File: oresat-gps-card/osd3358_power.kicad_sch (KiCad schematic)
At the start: 52 parts, among them Q6 MMBT2907, U1 OSD3358-512M-BSM, U10 SN74LVC1G07DCK, U13 RCLAMP0504FB, U14 TLVH431

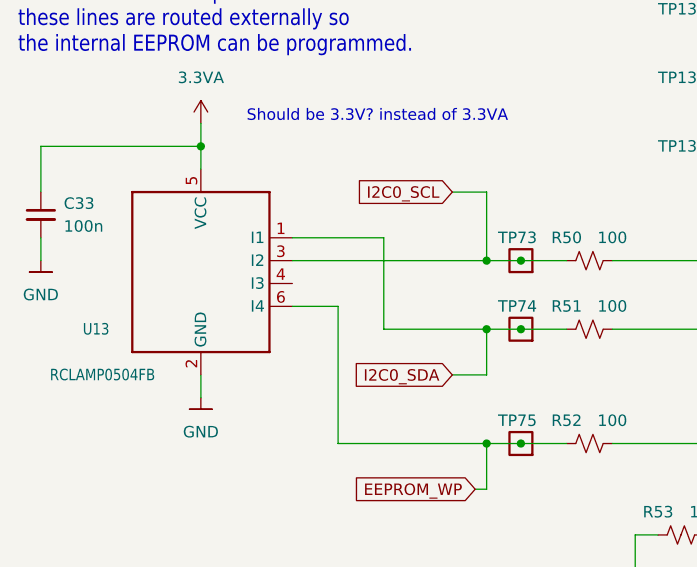
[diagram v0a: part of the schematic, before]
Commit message: GPS card design review changes and issue fixes
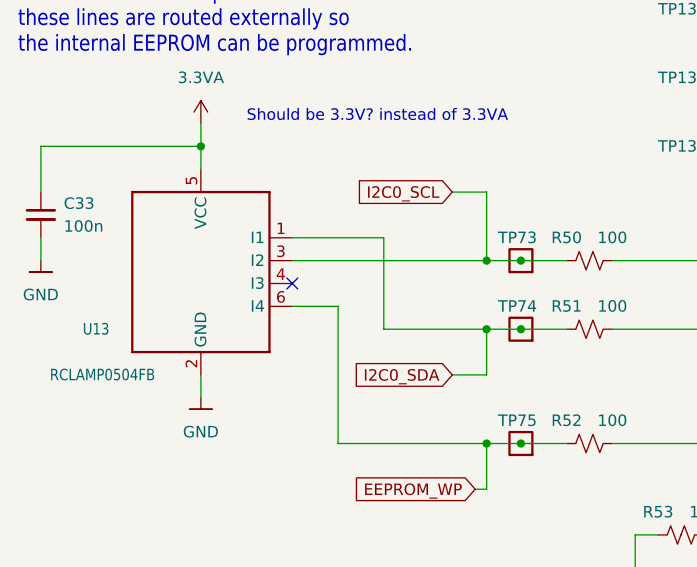
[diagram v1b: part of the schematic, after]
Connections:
- no-connect marks 0 -> 1
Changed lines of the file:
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@@
   (junction (at 175.26 55.88) (diameter 0) (color 0 0 0 0)
   )
+  (no_connect (at 48.26 187.96))
   (wire (pts (xy 355.6 58.42) (xy 355.6 63.5))
     (stroke (width 0) (type default) (color 0 0 0 0))
